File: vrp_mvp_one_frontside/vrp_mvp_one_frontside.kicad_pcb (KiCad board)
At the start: 2 copper layers, 77 x 150 mm, 70 parts, among them J1 Micro_SD_Card, J2 BACKSIDE_INTERFACE_1, J3 VIB_OUT, J4 USB_C_Receptacle_USB2.0_16P, J6 DEBUG, J7 BACKSIDE_INTERFACE_2, J8 SJ3-35094BG, Q1 MMBT2222A, Q2 MMBT2222A, SW1 SEND, SW10 TWO, SW11 THREE, SW12 FOUR, SW13 FIVE, SW14 SIX, SW15 SEVEN, SW16 EIGHT, SW17 NINE, SW18 ALPHA, SW19 BETA, SW2 END, SW20 ZERO, SW3 PAGE, SW4 CLR, SW5 POUND, SW6 UP, SW7 DOWN, SW8 ASTERISK, SW9 ONE, U2 NHD-C0220BIZ, U3 ATSAMD21G18A-A, U4 TLV320AIC3104IRHBT, U5 SN74CB3Q3257PWR

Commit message: more codec stuff
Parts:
- added C16: 100uF, Capacitor_SMD:C_0805_2012Metric_Pad1.18x1.45mm_HandSolder, F.Cu at (160.5, 56.0)
- added C17: 100uF, Capacitor_SMD:C_0805_2012Metric_Pad1.18x1.45mm_HandSolder, F.Cu at (160.5, 59.0)
- added C18: 220uF, Capacitor_SMD:C_0805_2012Metric_Pad1.18x1.45mm_HandSolder, F.Cu at (160.5, 62.0)
- added LS1: AST-01508MR-R, AST_01508MR_R:SPKR_AST-01508MR-R, F.Cu at (101.7, 28.5)
- added MK1: CMB-6544PF, CMB_6544PF:MIC_CMB-6544PF, F.Cu at (131.0, 154.5)
- moved J6 12.6 mm to (179.0, 54.4)
- moved U2 2.10 mm to (103.5, 48.1)
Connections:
- C1 pad 1: GND -> 1.8V
- C10 pad 1: GND -> 1.8V
- C11 pad 1: GND -> 1.8V
- C12 pad 1: GND -> 1.8V
- C13 pad 1: GND -> 1.8V
- C14 pad 2: GND -> 1.8V
- C15 pad 1: GND -> 1.8V
- C19 pad 2: GND -> 1.8V
- C20 pad 2: GND -> 1.8V
- C21 pad 2: GND -> 1.8V
- C23 pad 2: GND -> 1.8V
- C3 pad 1: GND -> 1.8V
- C4 pad 2: GND -> 1.8V
- C5 pad 1: GND -> unconnected-(C5-Pad1)
- C6 pad 1: GND -> 1.8V
- C7 pad 2: GND -> 1.8V
- C8 pad 1: GND -> 1.8V
- C9 pad 1: GND -> 1.8V
- H1 pad 1: GND -> 1.8V
- H2 pad 1: GND -> 1.8V
- H3 pad 1: GND -> 1.8V
- H4 pad 1: GND -> 1.8V
- J1 pad 6: GND -> 1.8V
- J1 pad 9: GND -> 1.8V
- J2 pad 1: GND -> 1.8V
- J2 pad 8: GND -> 1.8V
- J4 pad A1: GND -> 1.8V
- J4 pad A12: GND -> 1.8V
- J4 pad B1: GND -> 1.8V
- J4 pad B12: GND -> 1.8V
- J4 pad S1: GND -> 1.8V
- J6 pad 1: GND -> 1.8V
- J7 pad 1: GND -> 1.8V
- J7 pad 8: GND -> 1.8V
- J8 pad 1: unconnected-(J8-Pad1) -> HEADSET_MIC+
- J8 pad 2: unconnected-(J8-Pad2) -> HEAD_PHONE_L
- J8 pad 3: unconnected-(J8-Pad3) -> HEAD_PHONE_R
- J8 pad 4: unconnected-(J8-Pad4) -> 1.8V
- Q1 pad 2: GND -> 1.8V
- Q2 pad 2: GND -> 1.8V
- R1 pad 1: GND -> 1.8V
- R11 pad 2: GND -> 1.8V
- R2 pad 1: GND -> 1.8V
- R38 pad 1: GND -> 1.8V
- R39 pad 1: GND -> 1.8V
- R40 pad 1: GND -> 1.8V
- R8 pad 2: GND -> 1.8V
- U2 pad 4: GND -> 1.8V
- U3 pad 18: GND -> 1.8V
- U3 pad 35: GND -> 1.8V
- U3 pad 42: GND -> 1.8V
- U4 pad 14: unconnected-(U4-MIC2L/LINE2L/MICDET-Pad14) -> HEADSET_MIC+
- U4 pad 15: unconnected-(U4-MICBIAS-Pad15) -> Net-(U4-MICBIAS)
- U4 pad 16: unconnected-(U4-MIC2R/LINE2R-Pad16) -> Net-(U4-MIC2R/LINE2R)
- U4 pad 17: GND -> 1.8V
- U4 pad 19: unconnected-(U4-HPLOUT-Pad19) -> Net-(U4-HPLOUT)
- U4 pad 21: GND -> 1.8V
- U4 pad 23: unconnected-(U4-HPROUT-Pad23) -> Net-(U4-HPROUT)
- U4 pad 26: GND -> 1.8V
- U4 pad 6: GND -> 1.8V
- U5 pad 15: GND -> 1.8V
- U5 pad 8: GND -> 1.8V
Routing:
- added copper zone on F.Cu, net 1.8V
- removed copper zone on F.Cu, net GND

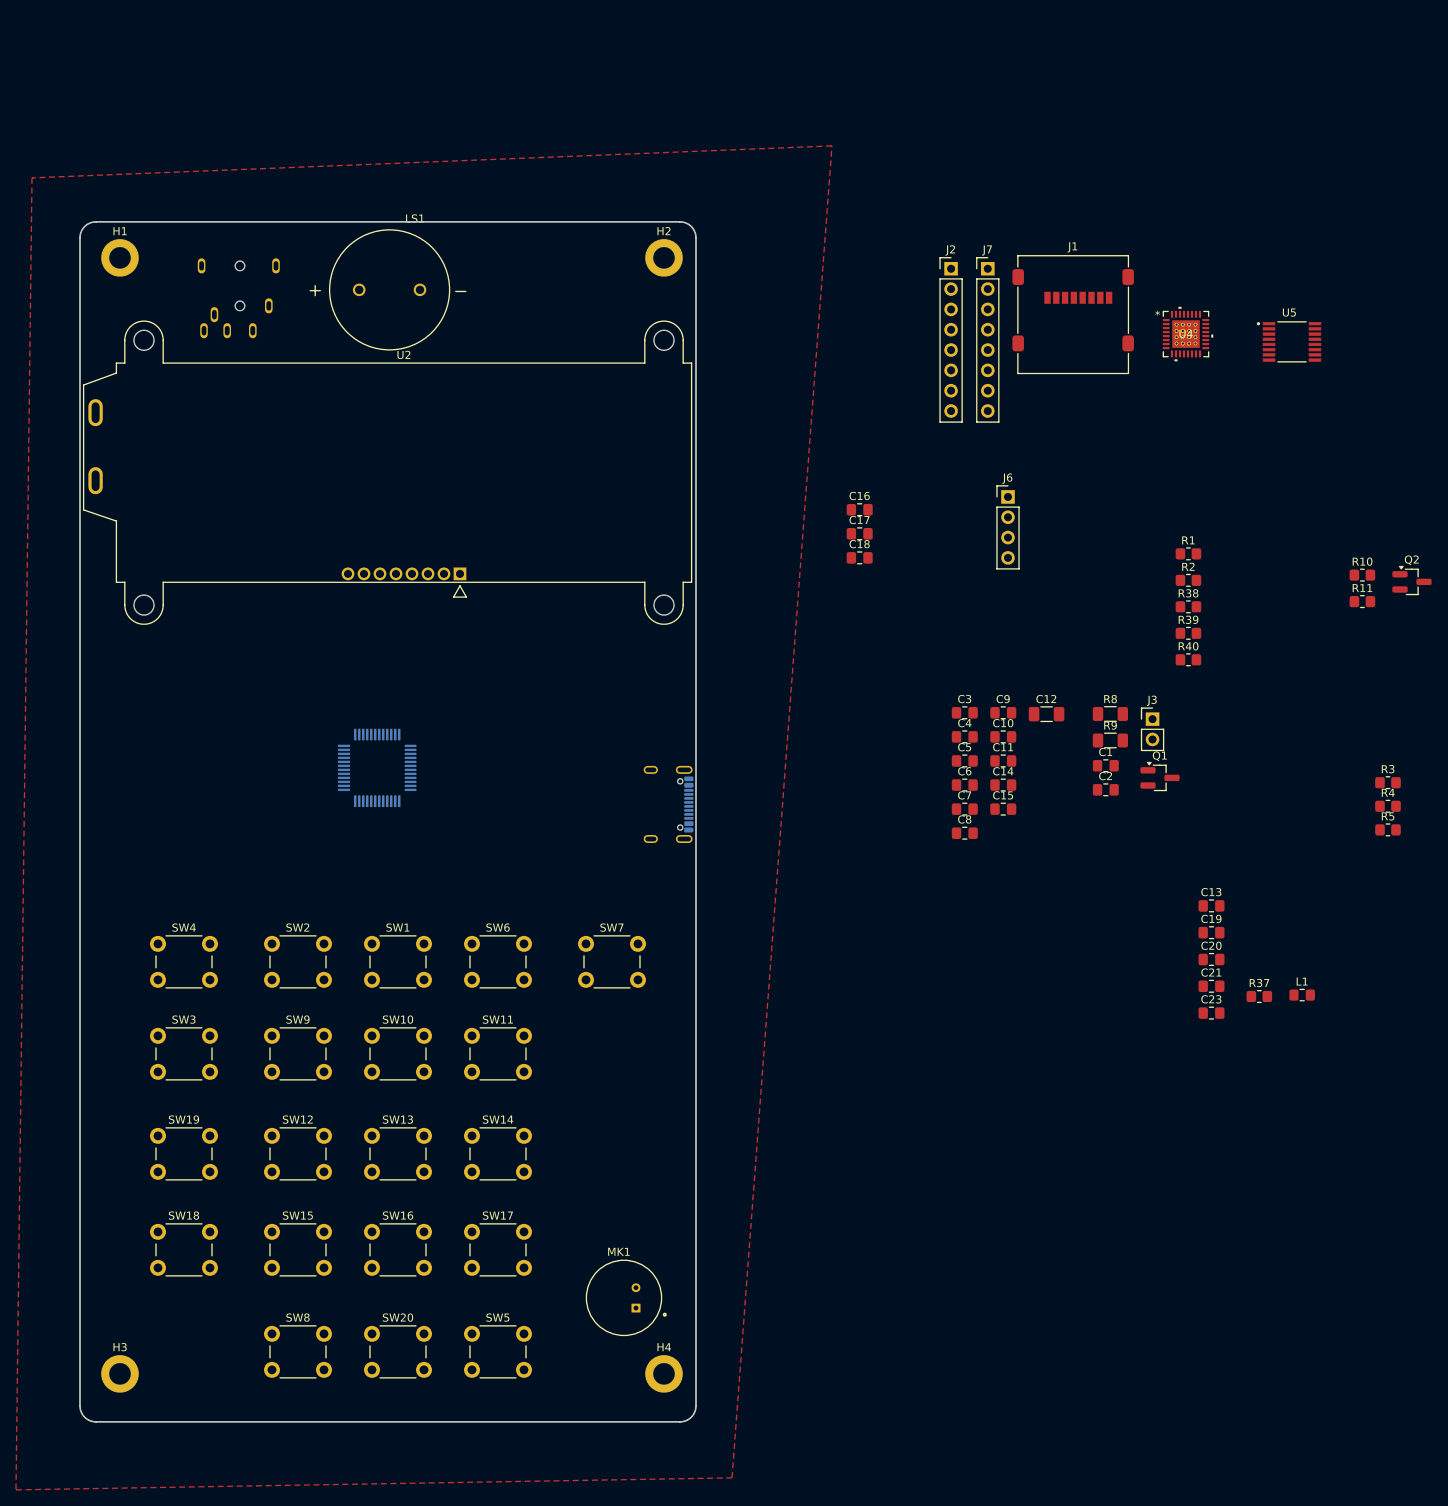
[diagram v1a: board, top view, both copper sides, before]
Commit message: audio, more routing, switched to lipo battery
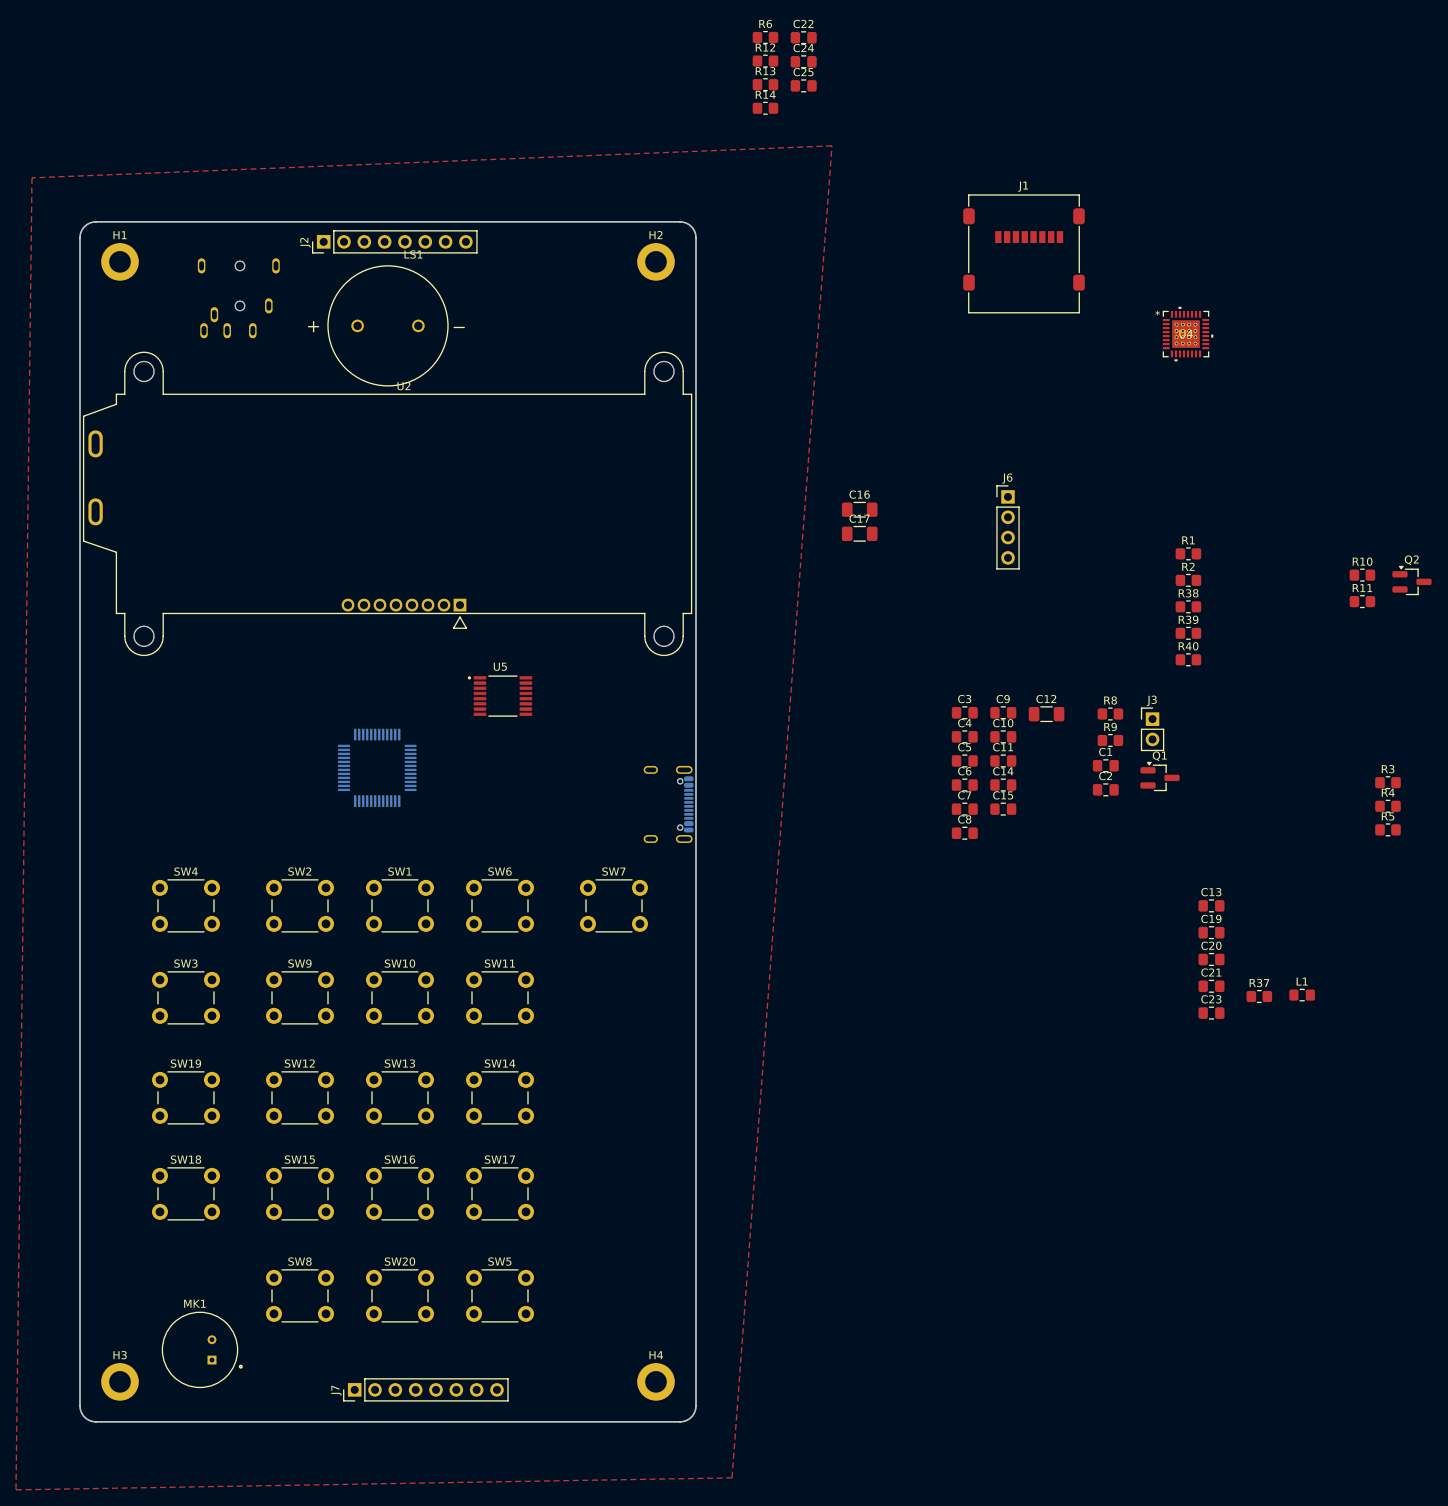
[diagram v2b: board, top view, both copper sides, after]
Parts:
- removed C18: 220uF, Capacitor_SMD:C_0805_2012Metric_Pad1.18x1.45mm_HandSolder
- added C22: 100nF, Capacitor_SMD:C_0805_2012Metric_Pad1.18x1.45mm_HandSolder, F.Cu at (153.5, -3.02)
- added C24: 100nF, Capacitor_SMD:C_0805_2012Metric_Pad1.18x1.45mm_HandSolder, F.Cu at (153.5, -0.01)
- added C25: 100nF, Capacitor_SMD:C_0805_2012Metric_Pad1.18x1.45mm_HandSolder, F.Cu at (153.5, 3.00)
- added R12: 1k, Resistor_SMD:R_0805_2012Metric_Pad1.20x1.40mm_HandSolder, F.Cu at (148.7, -0.10)
- added R13: 1k, Resistor_SMD:R_0805_2012Metric_Pad1.20x1.40mm_HandSolder, F.Cu at (148.7, 2.85)
- added R14: 1k, Resistor_SMD:R_0805_2012Metric_Pad1.20x1.40mm_HandSolder, F.Cu at (148.7, 5.80)
- added R6: 10k, Resistor_SMD:R_0805_2012Metric_Pad1.20x1.40mm_HandSolder, F.Cu at (148.7, -3.05)
- C16, C17: footprint Capacitor_SMD:C_0805_2012Metric_Pad1.18x1.45mm_HandSolder -> Capacitor_SMD:C_1206_3216Metric_Pad1.33x1.80mm_HandSolder
- R8, R9: footprint Resistor_SMD:R_1206_3216Metric_Pad1.30x1.75mm_HandSolder -> Resistor_SMD:R_0805_2012Metric_Pad1.20x1.40mm_HandSolder
- moved J7 160.9 mm to (97.3, 166.0), turned to 90 degrees
- moved U5 108.1 mm to (115.9, 79.3)
- moved J2 78.5 mm to (93.5, 22.5), turned to 90 degrees
- moved MK1 53.4 mm to (78.0, 161.0)
- moved J1 9.77 mm to (181.0, 24.0)
- moved SW1 7.00 mm to (99.8, 103.2)
- moved SW10 7.00 mm to (99.8, 114.8)
- moved SW11 7.00 mm to (112.2, 114.8)
- moved SW12 7.00 mm to (87.2, 127.2)
- moved SW13 7.00 mm to (99.8, 127.2)
- moved SW14 7.00 mm to (112.2, 127.2)
- moved SW15 7.00 mm to (87.2, 139.2)
- moved SW16 7.00 mm to (99.8, 139.2)
- moved SW17 7.00 mm to (112.2, 139.2)
- moved SW18 7.00 mm to (73.0, 139.2)
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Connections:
- net 5V renamed VBAT+
- C1 pad 1: 1.8V -> GND
- C10 pad 1: 1.8V -> GND
- C11 pad 1: 1.8V -> GND
- C12 pad 1: 1.8V -> GND
- C13 pad 1: 1.8V -> GND
- C14 pad 2: 1.8V -> GND
- C15 pad 1: 1.8V -> GND
- C19 pad 2: 1.8V -> GND
- C20 pad 2: 1.8V -> GND
- C21 pad 2: 1.8V -> GND
- C23 pad 2: 1.8V -> GND
- C3 pad 1: 1.8V -> GND
- C4 pad 2: 1.8V -> GND
- C5 pad 1: unconnected-(C5-Pad1) -> GND
- C6 pad 1: 1.8V -> GND
- C7 pad 2: 1.8V -> GND
- C8 pad 1: 1.8V -> GND
- C9 pad 1: 1.8V -> GND
- H1 pad 1: 1.8V -> GND
- H2 pad 1: 1.8V -> GND
- H3 pad 1: 1.8V -> GND
- H4 pad 1: 1.8V -> GND
- J1 pad 6: 1.8V -> GND
- J1 pad 9: 1.8V -> GND
- J2 pad 1: 1.8V -> GND
- J2 pad 8: 1.8V -> GND
- J4 pad A1: 1.8V -> GND
- J4 pad A12: 1.8V -> GND
- J4 pad B1: 1.8V -> GND
- J4 pad B12: 1.8V -> GND
- J4 pad S1: 1.8V -> GND
- J6 pad 1: 1.8V -> GND
- J7 pad 1: 1.8V -> GND
- J7 pad 2: unconnected-(J7-Pin_2-Pad2) -> I2S_MODEM_SCK
- J7 pad 3: unconnected-(J7-Pin_3-Pad3) -> I2S_MODEM_FS
- J7 pad 4: unconnected-(J7-Pin_4-Pad4) -> I2S_MODEM_DIN
- J7 pad 5: unconnected-(J7-Pin_5-Pad5) -> I2S_MODEM_DOUT
- J7 pad 7: unconnected-(J7-Pin_7-Pad7) -> LED_FLASH_ENABLE
- J7 pad 8: 1.8V -> GND
- J8 pad 4: 1.8V -> GND
- LS1 pad P: unconnected-(LS1-PadP) -> EAR_PIECE+
- Q1 pad 2: 1.8V -> GND
- Q1 pad 3: unconnected-(Q1-C-Pad3) -> LCD_BACKLIGHT_SINK
- Q2 pad 2: 1.8V -> GND
- R1 pad 1: 1.8V -> GND
- R11 pad 2: 1.8V -> GND
- R2 pad 1: 1.8V -> GND
- R38 pad 1: 1.8V -> GND
- R39 pad 1: 1.8V -> GND
- R40 pad 1: 1.8V -> GND
- R8 pad 2: 1.8V -> GND
- U2 pad 4: 1.8V -> GND
- U3 pad 18: 1.8V -> GND
- U3 pad 35: 1.8V -> GND
- U3 pad 39: unconnected-(U3-PA27-Pad39) -> LED_FLASH_ENABLE
- U3 pad 42: 1.8V -> GND
- U4 pad 10: unconnected-(U4-MIC1LP/LINE1LP-Pad10) -> Net-(U4-MIC1LP/LINE1LP)
- U4 pad 11: unconnected-(U4-MIC1LM/LINE1LM-Pad11) -> Net-(U4-MIC1LM/LINE1LM)
- U4 pad 12: unconnected-(U4-MIC1RP/LINE1RP-Pad12) -> Net-(U4-MIC1RP/LINE1RP)
- U4 pad 13: unconnected-(U4-MIC1RM/LINE1RM-Pad13) -> GND
- U4 pad 14: HEADSET_MIC+ -> unconnected-(U4-MIC2L/LINE2L/MICDET-Pad14)
- U4 pad 15: Net-(U4-MICBIAS) -> MIC_BIAS
- U4 pad 16: Net-(U4-MIC2R/LINE2R) -> unconnected-(U4-MIC2R/LINE2R-Pad16)
- U4 pad 17: 1.8V -> GND
- U4 pad 21: 1.8V -> GND
- U4 pad 26: 1.8V -> GND
- U4 pad 6: 1.8V -> GND
- U5 pad 15: 1.8V -> GND
- U5 pad 8: 1.8V -> GND

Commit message: more routing and part placement
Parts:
- added SW21: RESET, Button_Switch_THT:SW_PUSH_6mm, F.Cu at (68.0, 92.0)
- J4, U3: moved to F.Cu
- moved C24 179.4 mm to (70.5, 159.0)
- moved C22 178.7 mm to (72.0, 156.0), turned to 180 degrees
- moved Q2 160.2 mm to (74.5, 105.5)
- moved R10 159.1 mm to (69.5, 105.0)
- moved R11 154.1 mm to (73.0, 101.5), turned to 90 degrees
- moved R37 134.2 mm to (78.5, 92.0)
- moved J1 123.3 mm to (71.1, 79.9), turned to -90 degrees
- moved R4 120.5 mm to (108.0, 71.0), turned to 180 degrees
- moved R5 120.1 mm to (109.5, 69.0), turned to 180 degrees
- moved L1 119.9 mm to (98.0, 94.0), turned to 90 degrees
- moved C21 117.5 mm to (90.0, 89.0), turned to 180 degrees
- moved C23 116.5 mm to (95.5, 77.5), turned to 90 degrees
- moved C13 116.0 mm to (90.0, 86.5)
- moved R3 115.2 mm to (113.5, 67.5), turned to 180 degrees
- moved R39 113.3 mm to (124.0, 154.0), turned to 180 degrees
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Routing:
- added copper zone on B.Cu, net 1.8V
- removed copper zone on F.Cu, net 1.8V

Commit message: changes
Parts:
- removed J3: VIB_OUT, Connector_PinHeader_2.54mm:PinHeader_1x02_P2.54mm_Vertical
- added D2: STATUS, LED_SMD:LED_0805_2012Metric, F.Cu at (109.4, 22.0)
- added Q3: MMBT2222A, Package_TO_SOT_SMD:SOT-23_Handsoldering, F.Cu at (109.5, 30.5)
- added R15: 10k, Resistor_SMD:R_0805_2012Metric_Pad1.20x1.40mm_HandSolder, F.Cu at (84.0, 97.0)
- added R16: 100, Resistor_SMD:R_0805_2012Metric_Pad1.20x1.40mm_HandSolder, F.Cu at (107.5, 34.5)
- added R17: 10K, Resistor_SMD:R_0805_2012Metric_Pad1.20x1.40mm_HandSolder, F.Cu at (111.5, 34.5)
- added R18: 1k, Resistor_SMD:R_0805_2012Metric_Pad1.20x1.40mm_HandSolder, F.Cu at (112.5, 29.5)
- added R7: 10k, Resistor_SMD:R_0805_2012Metric_Pad1.20x1.40mm_HandSolder, F.Cu at (84.0, 93.0)
- moved R14 101.4 mm to (76.0, 29.0), turned to -90 degrees
- moved R13 100.2 mm to (70.5, 161.0), turned to 180 degrees
- moved R12 89.6 mm to (81.0, 154.0), turned to 180 degrees
- moved R10 70.9 mm to (135.5, 131.0), turned to 90 degrees
- moved R11 70.9 mm to (137.5, 131.0), turned to -90 degrees
- moved Q2 65.3 mm to (136.5, 126.0), turned to 90 degrees
- moved R6 30.2 mm to (118.5, 85.0), turned to 180 degrees
- moved R5 24.7 mm to (115.5, 93.0), turned to -90 degrees
- moved R4 23.5 mm to (117.5, 92.5), turned to -90 degrees
- moved R9 14.7 mm to (80.5, 74.0), turned to 90 degrees
- moved Q1 8.14 mm to (81.5, 69.0), turned to 90 degrees
- moved R8 7.52 mm to (82.5, 74.0), turned to -90 degrees
- moved SW21 6.32 mm to (70.0, 98.0)
- moved J6 6.11 mm to (103.1, 108.0)
- moved C23 5.00 mm to (95.5, 82.5), turned to 180 degrees
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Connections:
- J2 pad 5: MODEM_UART_TX -> MODEM_UART_RX
- J2 pad 6: MODEM_UART_RX -> MODEM_UART_TX
- J7 pad 3: I2S_MODEM_FS -> I2S_MODEM_DOUT
- J7 pad 5: I2S_MODEM_DOUT -> I2S_MODEM_FS
- J7 pad 6: unconnected-(J7-Pin_6-Pad6) -> CHARGE_STATUS
- R14 pad 2: unconnected-(R14-Pad2) -> MIC_BIAS
- R5 pad 2: I2C_SDL -> I2C_SCL
- U2 pad 2: I2C_SDL -> I2C_SCL
- U3 pad 10: unconnected-(U3-PA05-Pad10) -> MODEM_UART_TX
- U3 pad 11: unconnected-(U3-PA06-Pad11) -> MODEM_UART_RX
- U3 pad 21: SPI_MOSI -> SPI_CS_SD
- U3 pad 22: SPI_MISO -> SPI_MOSI
- U3 pad 24: SPI_CS_SD -> SPI_MISO
- U3 pad 41: unconnected-(U3-PA28-Pad41) -> CHARGE_STATUS
- U3 pad 47: unconnected-(U3-PB02-Pad47) -> BATT_SENSE
- U4 pad 29: unconnected-(U4-RIGHT_LOP-Pad29) -> EAR_PIECE+
- U4 pad 30: unconnected-(U4-RIGHT_LOM-Pad30) -> EAR_PIECE-
- U5 pad 4: I2S_CODEC_SCK -> I2S_CODEC_FS
- U5 pad 7: I2S_CODEC_FS -> I2S_CODEC_SCK
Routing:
- net MIC_BIAS: track 0.00 -> 208.1 mm, vias 0 -> 6
- net LED_FLASH_ENABLE: track 0.00 -> 206.5 mm, vias 0 -> 4
- net 3.3V: track 0.00 -> 194.1 mm, vias 0 -> 2
- net SW_COL_D: track 0.00 -> 187.8 mm, vias 0 -> 7
- net CHARGE_STATUS: track 0.00 -> 164.9 mm, vias 0 -> 6
- net SW_ROW_D: track 0.00 -> 154.7 mm, vias 0 -> 6
- net SW_ROW_E: track 0.00 -> 154.2 mm, vias 0 -> 5
- net I2S_MODEM_DOUT: track 0.00 -> 150.3 mm
- net SW_COL_C: track 0.00 -> 144.7 mm, vias 0 -> 9
- net I2S_MODEM_SCK: track 0.00 -> 142.9 mm, vias 0 -> 4
- net I2S_MODEM_DIN: track 0.00 -> 141.9 mm
- net I2S_MODEM_FS: track 0.00 -> 139.6 mm, vias 0 -> 2
- net SW_ROW_B: track 0.00 -> 132.5 mm, vias 0 -> 7
- net SW_COL_A: track 0.00 -> 131.2 mm, vias 0 -> 2
- net SW_COL_B: track 0.00 -> 119.3 mm, vias 0 -> 8
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- added copper zone on B.Cu, net GND
- removed copper zone on B.Cu, net 1.8V
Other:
- board text added: "STATUS"

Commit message: board almost finalized
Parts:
- moved R6 1.80 mm to (120.0, 86.0), turned to -90 degrees
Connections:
- U3 pad 48: unconnected-(U3-PB03-Pad48) -> LED_STATUS
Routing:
- net 3.3V: track 194.1 -> 356.8 mm, vias 2 -> 12
- net LED_STATUS: track 0.00 -> 84.8 mm, vias 0 -> 4
- net LED_FLASH_ENABLE: track 206.5 -> 126.4 mm
- net EAR_PIECE+: track 7.18 -> 86.8 mm, vias 0 -> 2
- net VBAT+: track 0.00 -> 77.5 mm, vias 0 -> 2
- net EAR_PIECE-: track 6.81 -> 81.0 mm, vias 0 -> 2
- net HEADSET_MIC+: track 32.9 -> 106.7 mm, vias 0 -> 4
- net Net-(U4-HPLOUT): track 71.4 -> 138.5 mm
- net Net-(U4-HPROUT): track 70.1 -> 134.3 mm
- net MODEM_UART_TX: track 46.0 -> 88.1 mm
- net MODEM_UART_RX: track 44.6 -> 86.3 mm
- net I2C_SDA: track 35.6 -> 72.2 mm
- net I2C_SCL: track 33.4 -> 60.5 mm
- net Net-(D2-K): track 0.00 -> 18.6 mm
- net GND: track 63.7 -> 81.1 mm, vias 38 -> 58
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
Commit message: very close to authoring rev 0
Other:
- board text added: "3.3V"
- board text added: "GND"
- board text added: "SDIO"
- board text added: "SWCLK"
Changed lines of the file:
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@@
 		(layer "Edge.Cuts")
+	)
+	(gr_text "GND"
+		(at 103.5 106.5 90)
+		(layer "F.SilkS")
+		(effects
+			(font
+				(size 1 1)
+				(thickness 0.125)
+			)
+			(justify left bottom)
+		)
 	)
 	(gr_text "STATUS"
@@
 		(layer "F.SilkS")
 		(effects
+			(font
+				(size 1 1)
+				(thickness 0.125)
+			)
+			(justify left bottom)
+		)
+	)
+	(gr_text "SDIO"
+		(at 96 106.5 90)
+		(layer "F.SilkS")
+		(effects
+			(font
+				(size 1 1)
+				(thickness 0.125)
+			)
+			(justify left bottom)
+		)
+	)
+	(gr_text "3.3V"
+		(at 101 106.5 90)
+		(layer "F.SilkS")
+		(effects
+			(font
+				(size 1 1)
+				(thickness 0.125)
+			)
+			(justify left bottom)
+		)
+	)
+	(gr_text "SWCLK"
+		(at 98.5 106.5 90)
+		(layer "F.SilkS")
+		(effects
